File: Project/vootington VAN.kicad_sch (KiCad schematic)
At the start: 105 parts, among them U4 SLSS49E-3, U5 SLSS49E-3

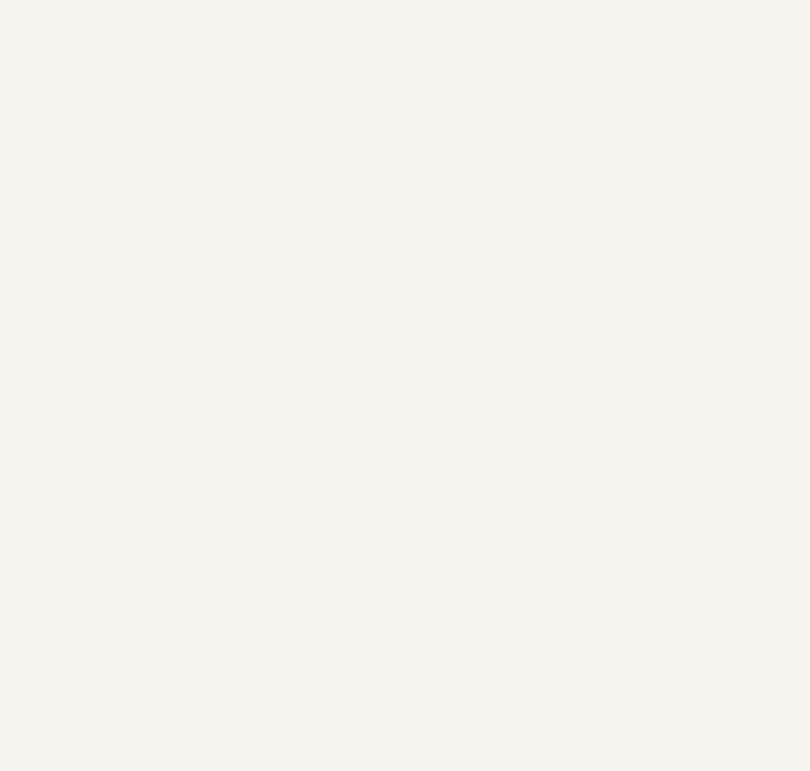
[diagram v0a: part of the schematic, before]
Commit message: created plates and production files for protos
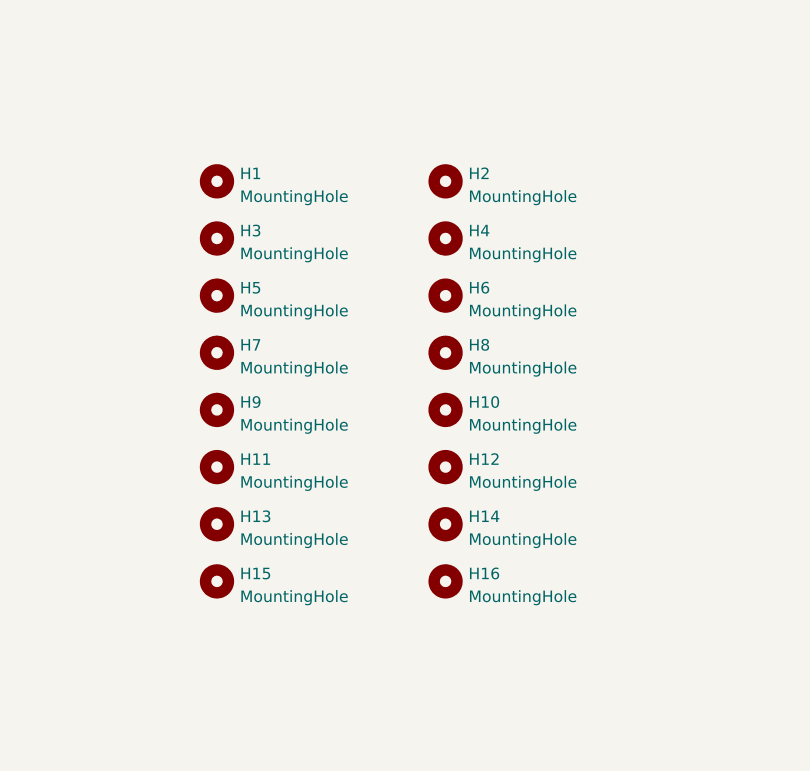
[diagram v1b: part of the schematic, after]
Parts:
- added H1, H10, H11, H12, H13, H14, H15, H16, H2, H3, H4, H5, H6, H7, H8, H9: MountingHole, cipulot_parts:HOLE_M2, symbol Mechanical:MountingHole
